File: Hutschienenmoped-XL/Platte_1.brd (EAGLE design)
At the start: 107.1 x 76.2 mm, 0 parts

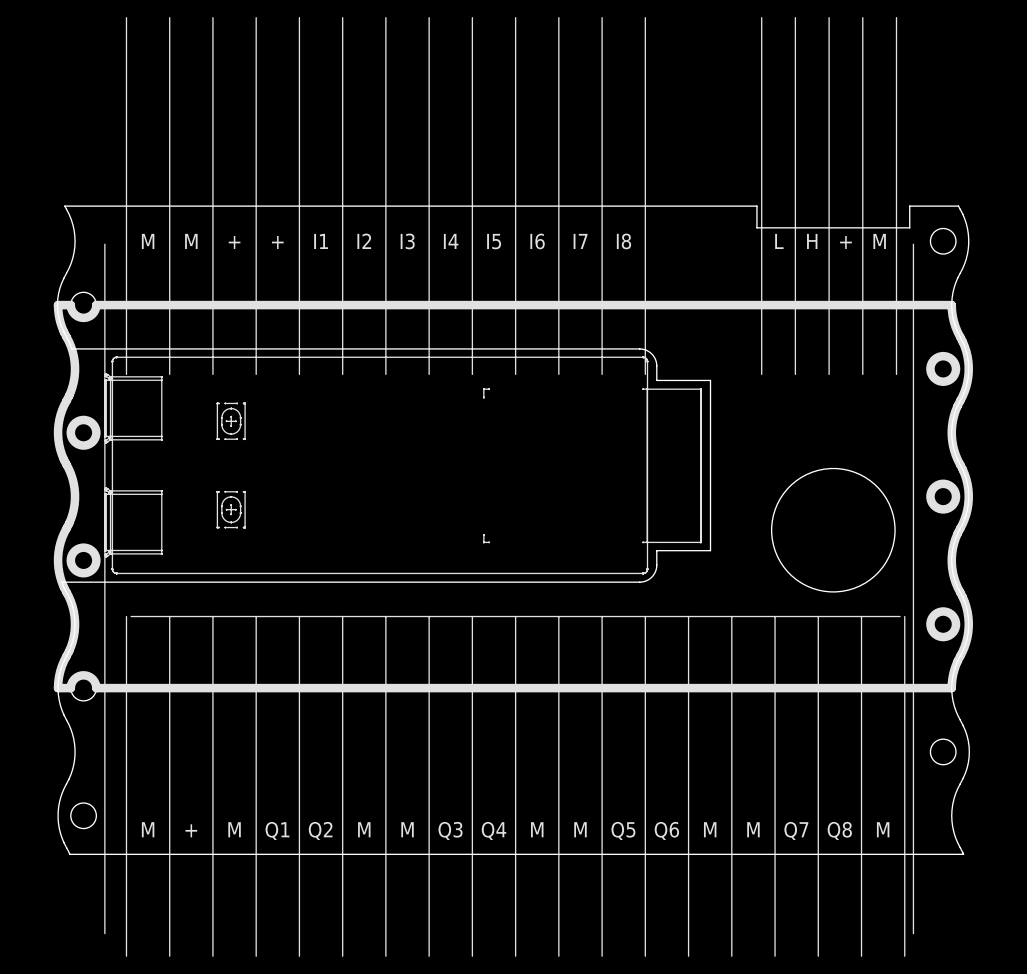
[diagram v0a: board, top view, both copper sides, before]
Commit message: Update wire coordinates and add new wires and circles.
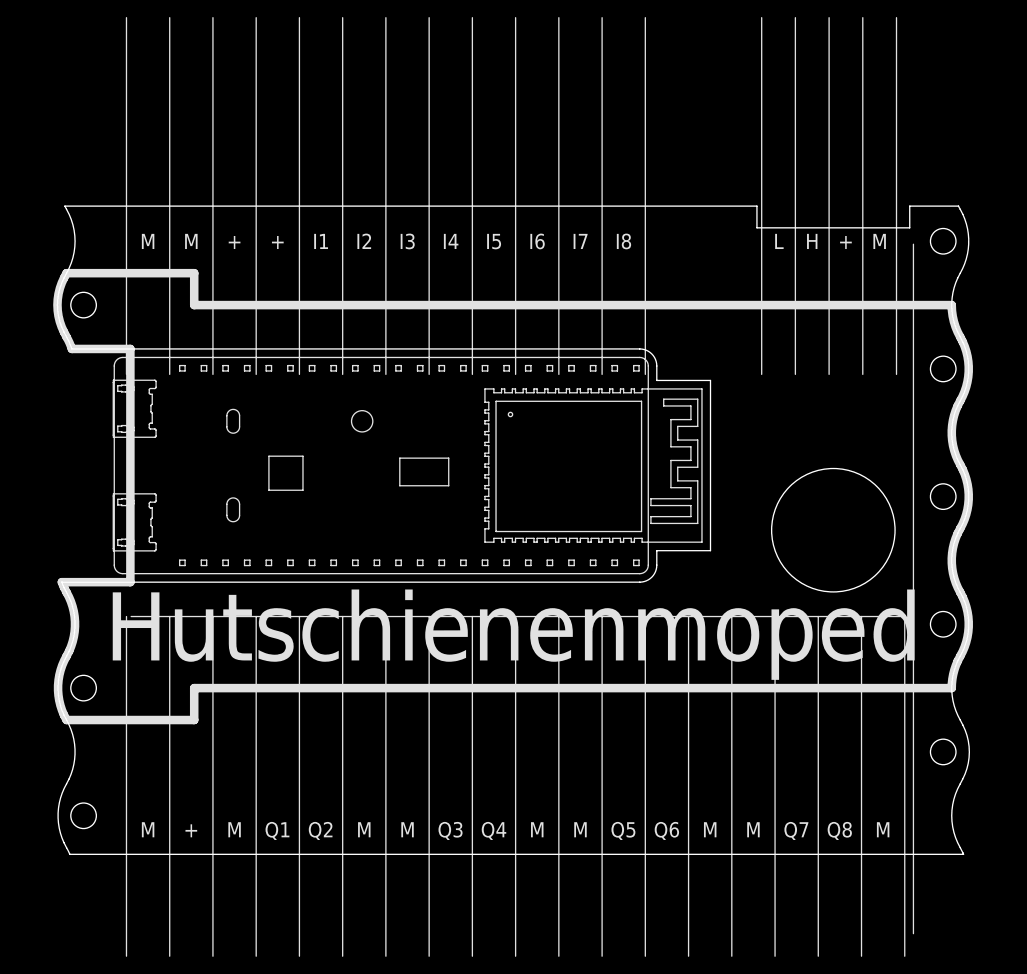
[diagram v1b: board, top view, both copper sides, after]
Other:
- board text added: "Hutschienenmoped"
